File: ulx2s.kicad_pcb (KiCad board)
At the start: 4 copper layers, 35.6 x 61 mm, 11 parts, among them J1 Conn_01x24, J2 Conn_01x24, J3 Micro_SD_Card_Det, J4 USB_OTG, J5 Conn_01x06, SW1 SW_Push, SW2 SW_Push, SW3 SW_Push, SW4 SW_Push, SW5 SW_Push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

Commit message: LEDs
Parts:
- added D0: RED, LEDs:LED_0805, F.Cu at (168.9, 101.6)
- added D1: RED, LEDs:LED_0805, F.Cu at (168.9, 99.1)
- added D2: RED, LEDs:LED_0805, F.Cu at (168.9, 96.5)
- added D3: RED, LEDs:LED_0805, F.Cu at (168.9, 94.0)
- added D4: RED, LEDs:LED_0805, F.Cu at (148.6, 101.6)
- added D5: RED, LEDs:LED_0805, F.Cu at (148.6, 99.1)
- added D6: RED, LEDs:LED_0805, F.Cu at (148.6, 96.5)
- added D7: RED, LEDs:LED_0805, F.Cu at (148.6, 94.0)
- added D8: RED, LEDs:LED_0805, F.Cu at (158.8, 85.1)

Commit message: flash chip
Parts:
- added U1: SST25VF032B, SOA008-150mil:SOA008-150mil, F.Cu at (148.6, 120.7)
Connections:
- J5 pad 1: (no net) -> +3V3
- J5 pad 2: (no net) -> GND
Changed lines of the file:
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@@
 (kicad_pcb (version 4) (host pcbnew 4.0.7+dfsg1-1)
   (general
-    (links 30)
-    (no_connects 30)
+    (links 32)
+    (no_connects 32)
     (area 140.894999 81.204999 176.605001 142.315001)
     (thickness 1.6)
@@
     (tracks 0)
     (zones 0)
-    (modules 20)
+    (modules 21)
     (nets 13)
   )
@@
       (effects (font (size 1 1) (thickness 0.15)) (justify mirror))
     )
-    (pad 1 thru_hole rect (at 0 0 270) (size 1.7 1.7) (drill 1) (layers *.Cu *.Mask))
-    (pad 2 thru_hole oval (at 0 -2.54 270) (size 1.7 1.7) (drill 1) (layers *.Cu *.Mask))
+    (pad 1 thru_hole rect (at 0 0 270) (size 1.7 1.7) (drill 1) (layers *.Cu *.Mask)
+      (net 2 +3V3))
+    (pad 2 thru_hole oval (at 0 -2.54 270) (size 1.7 1.7) (drill 1) (layers *.Cu *.Mask)
+      (net 1 GND))
     (pad 3 thru_hole oval (at 0 -5.08 270) (size 1.7 1.7) (drill 1) (layers *.Cu *.Mask))
     (pad 4 thru_hole oval (at 0 -7.62 270) (size 1.7 1.7) (drill 1) (layers *.Cu *.Mask))
@@
     )
   )
+  (module SOA008-150mil:SOA008-150mil (layer F.Cu)
+    (at 148.59 120.65 90)
+    (descr "Cypress SOA008 SOIC-8 150 mil")
+    (tags "SOA008 SOIC-8 1.27 150 mil")
+    (attr smd)
+    (fp_text reference U1 (at -2.54 4.064 360) (layer F.SilkS)
+      (effects (font (size 1 1) (thickness 0.15)))
+    )
+    (fp_text value SST25VF032B (at 4.318 5.588 360) (layer F.Fab)
+      (effects (font (size 1 1) (thickness 0.15)))
+    )
+    (fp_circle (center -0.9525 -2.286) (end -0.889 -2.2225) (layer F.SilkS) (width 0.15))
+    (fp_line (start -1.778 2.54) (end -1.778 -2.54) (layer F.SilkS) (width 0.15))
+    (fp_line (start -1.27 -2.54) (end -1.27 2.54) (layer F.SilkS) (width 0.15))
+    (fp_line (start -0.95 -2.45) (end 1.95 -2.45) (layer F.Fab) (width 0.15))
+    (fp_line (start 1.95 -2.45) (end 1.95 2.45) (layer F.Fab) (width 0.15))
+    (fp_line (start 1.95 2.45) (end -1.95 2.45) (layer F.Fab) (width 0.15))
+    (fp_line (start -1.95 2.45) (end -1.95 -1.45) (layer F.Fab) (width 0.15))
+    (fp_line (start -1.95 -1.45) (end -0.95 -2.45) (layer F.Fab) (width 0.15))
+    (fp_line (start -3.75 -2.75) (end -3.75 2.75) (layer F.CrtYd) (width 0.05))
+    (fp_line (start 3.75 -2.75) (end 3.75 2.75) (layer F.CrtYd) (width 0.05))
+    (fp_line (start -3.75 -2.75) (end 3.75 -2.75) (layer F.CrtYd) (width 0.05))
+    (fp_line (start -3.75 2.75) (end 3.75 2.75) (layer F.CrtYd) (width 0.05))
+    (fp_line (start -2.075 -2.575) (end -2.075 -2.525) (layer F.SilkS) (width 0.15))
+    (fp_line (start 2.075 -2.575) (end 2.075 -2.43) (layer F.SilkS) (width 0.15))
+    (fp_line (start 2.075 2.575) (end 2.075 2.43) (layer F.SilkS) (width 0.15))
+    (fp_line (start -2.075 2.575) (end -2.075 2.43) (layer F.SilkS) (width 0.15))
+    (fp_line (start -2.075 -2.575) (end 2.075 -2.575) (layer F.SilkS) (width 0.15))
+    (fp_line (start -2.075 2.575) (end 2.075 2.575) (layer F.SilkS) (width 0.15))
+    (fp_line (start -2.075 -2.525) (end -3.475 -2.525) (layer F.SilkS) (width 0.15))
+    (pad 1 smd rect (at -2.7 -1.905 90) (size 1.55 0.6) (layers F.Cu F.Paste F.Mask))
+    (pad 2 smd oval (at -2.7 -0.635 90) (size 1.55 0.6) (layers F.Cu F.Paste F.Mask))
+    (pad 3 smd oval (at -2.7 0.635 90) (size 1.55 0.6) (layers F.Cu F.Paste F.Mask))
+    (pad 4 smd oval (at -2.7 1.905 90) (size 1.55 0.6) (layers F.Cu F.Paste F.Mask))
+    (pad 5 smd oval (at 2.7 1.905 90) (size 1.55 0.6) (layers F.Cu F.Paste F.Mask))
+    (pad 6 smd oval (at 2.7 0.635 90) (size 1.55 0.6) (layers F.Cu F.Paste F.Mask))
+    (pad 7 smd oval (at 2.7 -0.635 90) (size 1.55 0.6) (layers F.Cu F.Paste F.Mask))
+    (pad 8 smd oval (at 2.7 -1.905 90) (size 1.55 0.6) (layers F.Cu F.Paste F.Mask))
+    (model Housings_SOIC.3dshapes/SOIC-8_3.9x4.9mm_Pitch1.27mm.wrl
+      (at (xyz 0 0 0))
+      (scale (xyz 1 1 1))
+      (rotate (xyz 0 0 0))
+    )
+  )

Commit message: PCB: oscillator renamed FNETHE025
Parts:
- Y1: value Crystal_GND24 -> FNETHE025
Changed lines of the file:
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@@
       (effects (font (size 1 1) (thickness 0.15)))
     )
-    (fp_text value Crystal_GND24 (at 0 4 90) (layer F.Fab)
+    (fp_text value FNETHE025 (at 0 4 90) (layer F.Fab)
       (effects (font (size 1 1) (thickness 0.15)))
     )
@@
       (effects (font (size 1 1) (thickness 0.15)))
     )
-    (fp_text value SST25VF032B (at 4.318 5.588 360) (layer F.Fab)
-      (effects (font (size 1 1) (thickness 0.15)))
-    )
+    (fp_text value SST25VF032B (at 0 -3.81 90) (layer F.Fab)
+      (effects (font (size 1 1) (thickness 0.15)))
+    )

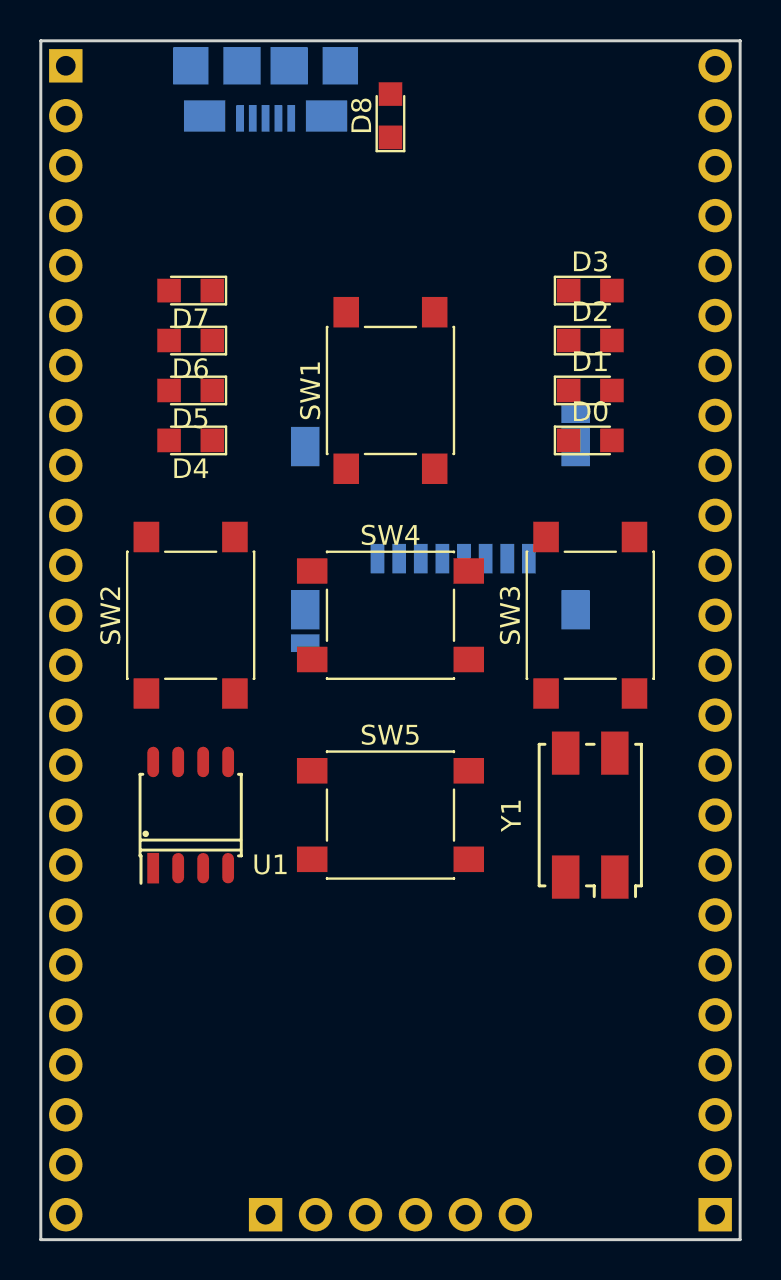
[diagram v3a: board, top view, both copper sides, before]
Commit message: fpga chip placed in the schematic "fpga" sheet and on the PCB.
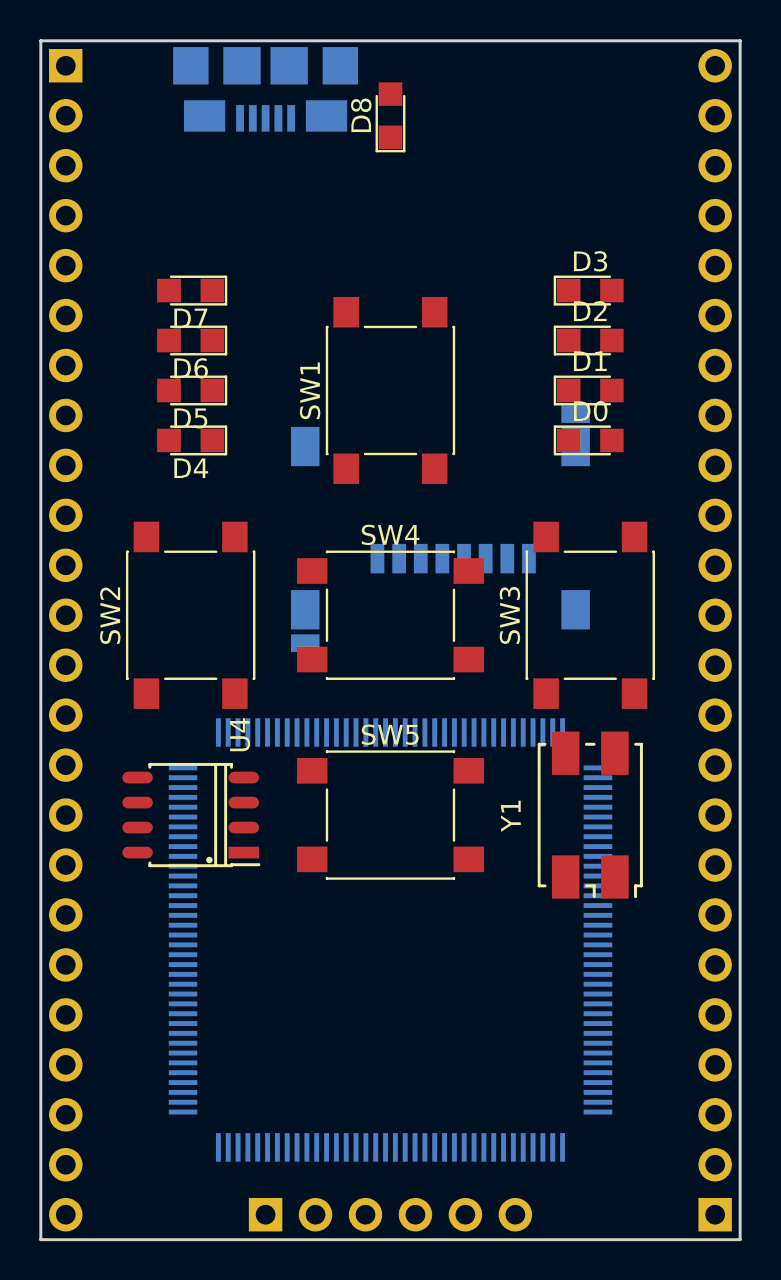
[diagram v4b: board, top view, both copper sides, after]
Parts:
- added U4: SST25VF032B, SOA008-150mil:SOA008-150mil, F.Cu at (148.6, 120.7)
- U1: value SST25VF032B -> LFXP2-xE-xTN144x; footprint SOA008-150mil:SOA008-150mil -> Housings_QFP:TQFP-144_20x20mm_Pitch0.5mm; moved to B.Cu
- moved U1 12.0 mm to (158.8, 127.0), turned to 270 degrees

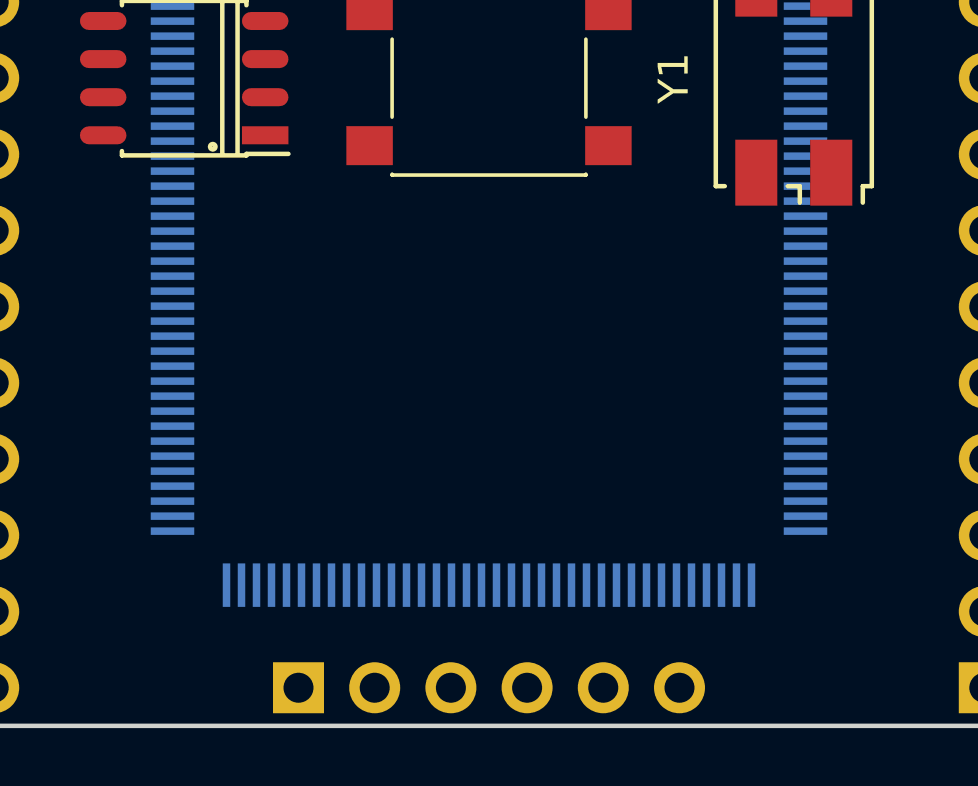
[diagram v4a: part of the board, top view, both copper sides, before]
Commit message: SRAM chip (not the correct one AS6C8016 but similar AS6C1616 which was readily available in kicad library)
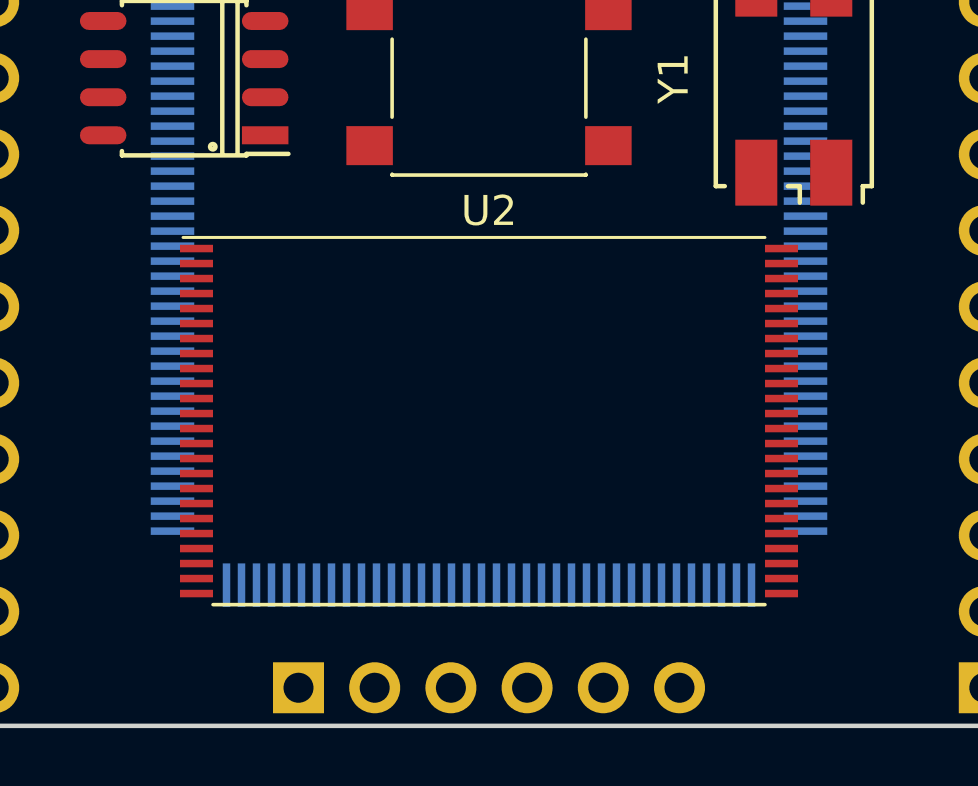
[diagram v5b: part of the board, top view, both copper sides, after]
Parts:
- added U2: AS6C1616, Housings_SSOP:TSOP-I-48_18.4x12mm_Pitch0.5mm, F.Cu at (158.8, 132.1)
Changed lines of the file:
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@@
 (kicad_pcb (version 4) (host pcbnew 4.0.7+dfsg1-1)
   (general
-    (links 32)
-    (no_connects 32)
+    (links 35)
+    (no_connects 35)
     (area 140.894999 81.204999 176.605001 142.315001)
     (thickness 1.6)
@@
     (tracks 0)
     (zones 0)
-    (modules 22)
+    (modules 23)
     (nets 13)
   )
@@
       (at (xyz 0 0 0))
       (scale (xyz 1 1 1))
+      (rotate (xyz 0 0 0))
+    )
+  )
+  (module Housings_SSOP:TSOP-I-48_18.4x12mm_Pitch0.5mm (layer F.Cu)
+    (at 158.75 132.08)
+    (descr "TSOP I, 32 pins, 18.4x8mm body (https://www.micron.com/~/media/documents/products/technical-note/nor-flash/tn1225_land_pad_design.pdf)")
+    (tags "TSOP I 32")
+    (attr smd)
+    (fp_text reference U2 (at 0 -7) (layer F.SilkS)
+      (effects (font (size 1 1) (thickness 0.15)))
+    )
+    (fp_text value AS6C1616 (at 0 7) (layer F.Fab)
+      (effects (font (size 1 1) (thickness 0.15)))
+    )
+    (fp_line (start -10.55 6.25) (end -10.55 -6.25) (layer F.CrtYd) (width 0.05))
+    (fp_line (start 10.55 6.25) (end -10.55 6.25) (layer F.CrtYd) (width 0.05))
+    (fp_line (start 10.55 -6.25) (end 10.55 6.25) (layer F.CrtYd) (width 0.05))
+    (fp_line (start -10.55 -6.25) (end 10.55 -6.25) (layer F.CrtYd) (width 0.05))
+    (fp_line (start -9.2 6.12) (end 9.2 6.12) (layer F.SilkS) (width 0.12))
+    (fp_line (start 9.2 -6.12) (end -10.2 -6.12) (layer F.SilkS) (width 0.1))
+    (fp_line (start -8.2 -6) (end -9.2 -5) (layer F.Fab) (width 0.1))
+    (fp_text user %R (at 0 0) (layer F.Fab)
+      (effects (font (size 1 1) (thickness 0.15)))
+    )
+    (fp_line (start 9.2 -6) (end 9.2 6) (layer F.Fab) (width 0.1))
+    (fp_line (start 9.2 6) (end -9.2 6) (layer F.Fab) (width 0.1))
+    (fp_line (start -9.2 6) (end -9.2 -5) (layer F.Fab) (width 0.1))
+    (fp_line (start -8.2 -6) (end 9.2 -6) (layer F.Fab) (width 0.1))
+    (pad 1 smd rect (at -9.75 -5.75) (size 1.1 0.25) (layers F.Cu F.Paste F.Mask))
+    (pad 25 smd rect (at 9.75 5.75) (size 1.1 0.25) (layers F.Cu F.Paste F.Mask))
+    (pad 2 smd rect (at -9.75 -5.25) (size 1.1 0.25) (layers F.Cu F.Paste F.Mask))
+    (pad 3 smd rect (at -9.75 -4.75) (size 1.1 0.25) (layers F.Cu F.Paste F.Mask))
+    (pad 4 smd rect (at -9.75 -4.25) (size 1.1 0.25) (layers F.Cu F.Paste F.Mask))
+    (pad 5 smd rect (at -9.75 -3.75) (size 1.1 0.25) (layers F.Cu F.Paste F.Mask))
+    (pad 6 smd rect (at -9.75 -3.25) (size 1.1 0.25) (layers F.Cu F.Paste F.Mask))
+    (pad 7 smd rect (at -9.75 -2.75) (size 1.1 0.25) (layers F.Cu F.Paste F.Mask))
+    (pad 8 smd rect (at -9.75 -2.25) (size 1.1 0.25) (layers F.Cu F.Paste F.Mask))
+    (pad 9 smd rect (at -9.75 -1.75) (size 1.1 0.25) (layers F.Cu F.Paste F.Mask))
+    (pad 10 smd rect (at -9.75 -1.25) (size 1.1 0.25) (layers F.Cu F.Paste F.Mask))
+    (pad 11 smd rect (at -9.75 -0.75) (size 1.1 0.25) (layers F.Cu F.Paste F.Mask))
+    (pad 12 smd rect (at -9.75 -0.25) (size 1.1 0.25) (layers F.Cu F.Paste F.Mask))
+    (pad 13 smd rect (at -9.75 0.25) (size 1.1 0.25) (layers F.Cu F.Paste F.Mask))
+    (pad 14 smd rect (at -9.75 0.75) (size 1.1 0.25) (layers F.Cu F.Paste F.Mask))
+    (pad 15 smd rect (at -9.75 1.25) (size 1.1 0.25) (layers F.Cu F.Paste F.Mask))
+    (pad 16 smd rect (at -9.75 1.75) (size 1.1 0.25) (layers F.Cu F.Paste F.Mask))
+    (pad 17 smd rect (at -9.75 2.25) (size 1.1 0.25) (layers F.Cu F.Paste F.Mask))
+    (pad 18 smd rect (at -9.75 2.75) (size 1.1 0.25) (layers F.Cu F.Paste F.Mask))
+    (pad 19 smd rect (at -9.75 3.25) (size 1.1 0.25) (layers F.Cu F.Paste F.Mask))
+    (pad 20 smd rect (at -9.75 3.75) (size 1.1 0.25) (layers F.Cu F.Paste F.Mask))
+    (pad 21 smd rect (at -9.75 4.25) (size 1.1 0.25) (layers F.Cu F.Paste F.Mask))
+    (pad 22 smd rect (at -9.75 4.75) (size 1.1 0.25) (layers F.Cu F.Paste F.Mask))
+    (pad 23 smd rect (at -9.75 5.25) (size 1.1 0.25) (layers F.Cu F.Paste F.Mask))
+    (pad 24 smd rect (at -9.75 5.75) (size 1.1 0.25) (layers F.Cu F.Paste F.Mask))
+    (pad 26 smd rect (at 9.75 5.25) (size 1.1 0.25) (layers F.Cu F.Paste F.Mask))
+    (pad 27 smd rect (at 9.75 4.75) (size 1.1 0.25) (layers F.Cu F.Paste F.Mask)
+      (net 1 GND))
+    (pad 28 smd rect (at 9.75 4.25) (size 1.1 0.25) (layers F.Cu F.Paste F.Mask))
+    (pad 29 smd rect (at 9.75 3.75) (size 1.1 0.25) (layers F.Cu F.Paste F.Mask))
+    (pad 30 smd rect (at 9.75 3.25) (size 1.1 0.25) (layers F.Cu F.Paste F.Mask))
+    (pad 31 smd rect (at 9.75 2.75) (size 1.1 0.25) (layers F.Cu F.Paste F.Mask))
+    (pad 32 smd rect (at 9.75 2.25) (size 1.1 0.25) (layers F.Cu F.Paste F.Mask))
+    (pad 33 smd rect (at 9.75 1.75) (size 1.1 0.25) (layers F.Cu F.Paste F.Mask))
+    (pad 34 smd rect (at 9.75 1.25) (size 1.1 0.25) (layers F.Cu F.Paste F.Mask))
+    (pad 35 smd rect (at 9.75 0.75) (size 1.1 0.25) (layers F.Cu F.Paste F.Mask))
+    (pad 36 smd rect (at 9.75 0.25) (size 1.1 0.25) (layers F.Cu F.Paste F.Mask))
+    (pad 37 smd rect (at 9.75 -0.25) (size 1.1 0.25) (layers F.Cu F.Paste F.Mask)
+      (net 2 +3V3))
+    (pad 38 smd rect (at 9.75 -0.75) (size 1.1 0.25) (layers F.Cu F.Paste F.Mask))
+    (pad 39 smd rect (at 9.75 -1.25) (size 1.1 0.25) (layers F.Cu F.Paste F.Mask))
+    (pad 40 smd rect (at 9.75 -1.75) (size 1.1 0.25) (layers F.Cu F.Paste F.Mask))
+    (pad 41 smd rect (at 9.75 -2.25) (size 1.1 0.25) (layers F.Cu F.Paste F.Mask))
+    (pad 42 smd rect (at 9.75 -2.75) (size 1.1 0.25) (layers F.Cu F.Paste F.Mask))
+    (pad 43 smd rect (at 9.75 -3.25) (size 1.1 0.25) (layers F.Cu F.Paste F.Mask))
+    (pad 44 smd rect (at 9.75 -3.75) (size 1.1 0.25) (layers F.Cu F.Paste F.Mask))
+    (pad 45 smd rect (at 9.75 -4.25) (size 1.1 0.25) (layers F.Cu F.Paste F.Mask))
+    (pad 46 smd rect (at 9.75 -4.75) (size 1.1 0.25) (layers F.Cu F.Paste F.Mask)
+      (net 1 GND))
+    (pad 47 smd rect (at 9.75 -5.25) (size 1.1 0.25) (layers F.Cu F.Paste F.Mask))
+    (pad 48 smd rect (at 9.75 -5.75) (size 1.1 0.25) (layers F.Cu F.Paste F.Mask))
+    (model ${KISYS3DMOD}/Housings_SSOP.3dshapes/TSOP-I-48_18.4x12mm_Pitch0.5mm.wrl
+      (at (xyz 0 0 0))
+      (scale (xyz 1 1 1))
